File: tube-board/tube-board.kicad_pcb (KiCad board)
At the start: 2 copper layers, 25.4 x 26.4 mm, 3 parts, among them J1 Conn_01x10_Male, J2 Conn_01x01_Male

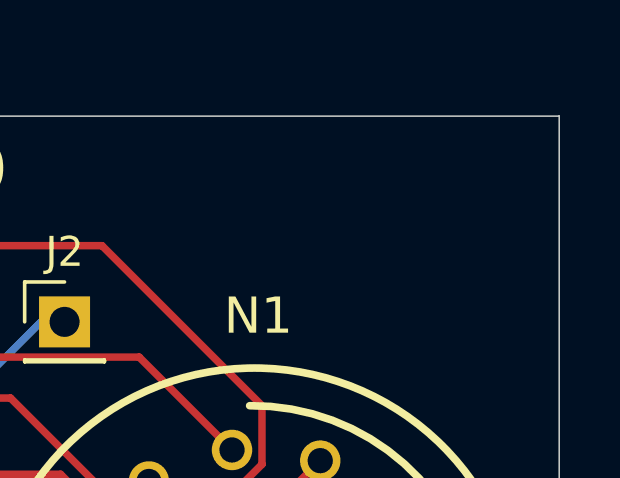
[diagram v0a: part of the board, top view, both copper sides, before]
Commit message: Add some mounting holes
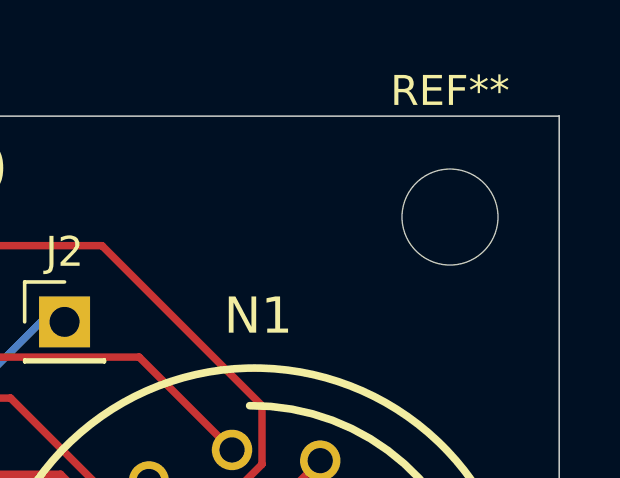
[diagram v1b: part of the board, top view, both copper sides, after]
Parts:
- added REF**: MountingHole_3.2mm_M3, MountingHole:MountingHole_3.2mm_M3, F.Cu at (100.5, 75.5)
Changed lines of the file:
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@@
-(kicad_pcb (version 20171130) (host pcbnew 5.1.12-1.fc35)
+(kicad_pcb (version 20171130) (host pcbnew 5.1.10)
   (general
     (thickness 1.6)
@@
     (tracks 42)
     (zones 0)
-    (modules 3)
+    (modules 4)
     (nets 14)
   )
@@
     (add_net "Net-(N1-PadRHDP)")
   )
+  (module MountingHole:MountingHole_3.2mm_M3 (layer F.Cu)
+    (at 100.5 75.5)
+    (descr "Mounting Hole 3.2mm, no annular, M3")
+    (tags "mounting hole 3.2mm no annular m3")
+    (attr virtual)
+    (fp_text reference REF** (at 0 -4.2) (layer F.SilkS)
+      (effects (font (size 1 1) (thickness 0.15)))
+    )
+    (fp_text value MountingHole_3.2mm_M3 (at 0 4.2) (layer F.Fab)
+      (effects (font (size 1 1) (thickness 0.15)))
+    )
+    (fp_text user %R (at 0.3 0) (layer F.Fab)
+      (effects (font (size 1 1) (thickness 0.15)))
+    )
+    (fp_circle (center 0 0) (end 3.2 0) (layer Cmts.User) (width 0.15))
+    (fp_circle (center 0 0) (end 3.45 0) (layer F.CrtYd) (width 0.05))
+    (pad 1 np_thru_hole circle (at 0 0) (size 3.2 3.2) (drill 3.2) (layers *.Cu *.Mask))
+  )
   (module nixies-us:IN-14 (layer F.Cu)
     (at 93.98 89.408 270)
@@
       (effects (font (size 1 1) (thickness 0.15)))
     )
+    (fp_line (start 1.8 -1.8) (end -1.8 -1.8) (layer F.CrtYd) (width 0.05))
+    (fp_line (start 1.8 1.8) (end 1.8 -1.8) (layer F.CrtYd) (width 0.05))
+    (fp_line (start -1.8 1.8) (end 1.8 1.8) (layer F.CrtYd) (width 0.05))
+    (fp_line (start -1.8 -1.8) (end -1.8 1.8) (layer F.CrtYd) (width 0.05))
+    (fp_line (start -1.33 -1.33) (end 0 -1.33) (layer F.SilkS) (width 0.12))
+    (fp_line (start -1.33 0) (end -1.33 -1.33) (layer F.SilkS) (width 0.12))
+    (fp_line (start -1.33 1.27) (end 1.33 1.27) (layer F.SilkS) (width 0.12))
+    (fp_line (start 1.33 1.27) (end 1.33 1.33) (layer F.SilkS) (width 0.12))
+    (fp_line (start -1.33 1.27) (end -1.33 1.33) (layer F.SilkS) (width 0.12))
+    (fp_line (start -1.33 1.33) (end 1.33 1.33) (layer F.SilkS) (width 0.12))
+    (fp_line (start -1.27 -0.635) (end -0.635 -1.27) (layer F.Fab) (width 0.1))
+    (fp_line (start -1.27 1.27) (end -1.27 -0.635) (layer F.Fab) (width 0.1))
+    (fp_line (start 1.27 1.27) (end -1.27 1.27) (layer F.Fab) (width 0.1))
+    (fp_line (start 1.27 -1.27) (end 1.27 1.27) (layer F.Fab) (width 0.1))
+    (fp_line (start -0.635 -1.27) (end 1.27 -1.27) (layer F.Fab) (width 0.1))
     (fp_text user %R (at 0 0 90) (layer F.Fab)
       (effects (font (size 1 1) (thickness 0.15)))
     )
-    (fp_line (start -0.635 -1.27) (end 1.27 -1.27) (layer F.Fab) (width 0.1))
-    (fp_line (start 1.27 -1.27) (end 1.27 1.27) (layer F.Fab) (width 0.1))
-    (fp_line (start 1.27 1.27) (end -1.27 1.27) (layer F.Fab) (width 0.1))
-    (fp_line (start -1.27 1.27) (end -1.27 -0.635) (layer F.Fab) (width 0.1))
-    (fp_line (start -1.27 -0.635) (end -0.635 -1.27) (layer F.Fab) (width 0.1))
-    (fp_line (start -1.33 1.33) (end 1.33 1.33) (layer F.SilkS) (width 0.12))
-    (fp_line (start -1.33 1.27) (end -1.33 1.33) (layer F.SilkS) (width 0.12))
-    (fp_line (start 1.33 1.27) (end 1.33 1.33) (layer F.SilkS) (width 0.12))
-    (fp_line (start -1.33 1.27) (end 1.33 1.27) (layer F.SilkS) (width 0.12))
-    (fp_line (start -1.33 0) (end -1.33 -1.33) (layer F.SilkS) (width 0.12))
-    (fp_line (start -1.33 -1.33) (end 0 -1.33) (layer F.SilkS) (width 0.12))
-    (fp_line (start -1.8 -1.8) (end -1.8 1.8) (layer F.CrtYd) (width 0.05))
-    (fp_line (start -1.8 1.8) (end 1.8 1.8) (layer F.CrtYd) (width 0.05))
-    (fp_line (start 1.8 1.8) (end 1.8 -1.8) (layer F.CrtYd) (width 0.05))
-    (fp_line (start 1.8 -1.8) (end -1.8 -1.8) (layer F.CrtYd) (width 0.05))
     (pad 1 thru_hole rect (at 0 0) (size 1.7 1.7) (drill 1) (layers *.Cu *.Mask)
       (net 11 "Net-(J2-Pad1)"))
@@
       (effects (font (size 1 1) (thickness 0.15)))
     )
+    (fp_line (start 1.8 -1.8) (end -1.8 -1.8) (layer F.CrtYd) (width 0.05))
+    (fp_line (start 1.8 24.65) (end 1.8 -1.8) (layer F.CrtYd) (width 0.05))
+    (fp_line (start -1.8 24.65) (end 1.8 24.65) (layer F.CrtYd) (width 0.05))
+    (fp_line (start -1.8 -1.8) (end -1.8 24.65) (layer F.CrtYd) (width 0.05))
+    (fp_line (start -1.33 -1.33) (end 0 -1.33) (layer F.SilkS) (width 0.12))
+    (fp_line (start -1.33 0) (end -1.33 -1.33) (layer F.SilkS) (width 0.12))
+    (fp_line (start -1.33 1.27) (end 1.33 1.27) (layer F.SilkS) (width 0.12))
+    (fp_line (start 1.33 1.27) (end 1.33 24.19) (layer F.SilkS) (width 0.12))
+    (fp_line (start -1.33 1.27) (end -1.33 24.19) (layer F.SilkS) (width 0.12))
+    (fp_line (start -1.33 24.19) (end 1.33 24.19) (layer F.SilkS) (width 0.12))
+    (fp_line (start -1.27 -0.635) (end -0.635 -1.27) (layer F.Fab) (width 0.1))
+    (fp_line (start -1.27 24.13) (end -1.27 -0.635) (layer F.Fab) (width 0.1))
+    (fp_line (start 1.27 24.13) (end -1.27 24.13) (layer F.Fab) (width 0.1))
+    (fp_line (start 1.27 -1.27) (end 1.27 24.13) (layer F.Fab) (width 0.1))
+    (fp_line (start -0.635 -1.27) (end 1.27 -1.27) (layer F.Fab) (width 0.1))
     (fp_text user %R (at 0 11.43 90) (layer F.Fab)
       (effects (font (size 1 1) (thickness 0.15)))
     )
-    (fp_line (start -0.635 -1.27) (end 1.27 -1.27) (layer F.Fab) (width 0.1))
-    (fp_line (start 1.27 -1.27) (end 1.27 24.13) (layer F.Fab) (width 0.1))
-    (fp_line (start 1.27 24.13) (end -1.27 24.13) (layer F.Fab) (width 0.1))
-    (fp_line (start -1.27 24.13) (end -1.27 -0.635) (layer F.Fab) (width 0.1))
-    (fp_line (start -1.27 -0.635) (end -0.635 -1.27) (layer F.Fab) (width 0.1))
-    (fp_line (start -1.33 24.19) (end 1.33 24.19) (layer F.SilkS) (width 0.12))
-    (fp_line (start -1.33 1.27) (end -1.33 24.19) (layer F.SilkS) (width 0.12))
-    (fp_line (start 1.33 1.27) (end 1.33 24.19) (layer F.SilkS) (width 0.12))
-    (fp_line (start -1.33 1.27) (end 1.33 1.27) (layer F.SilkS) (width 0.12))
-    (fp_line (start -1.33 0) (end -1.33 -1.33) (layer F.SilkS) (width 0.12))
-    (fp_line (start -1.33 -1.33) (end 0 -1.33) (layer F.SilkS) (width 0.12))
-    (fp_line (start -1.8 -1.8) (end -1.8 24.65) (layer F.CrtYd) (width 0.05))
-    (fp_line (start -1.8 24.65) (end 1.8 24.65) (layer F.CrtYd) (width 0.05))
-    (fp_line (start 1.8 24.65) (end 1.8 -1.8) (layer F.CrtYd) (width 0.05))
-    (fp_line (start 1.8 -1.8) (end -1.8 -1.8) (layer F.CrtYd) (width 0.05))
     (pad 10 thru_hole oval (at 0 22.86) (size 1.7 1.7) (drill 1) (layers *.Cu *.Mask)
       (net 1 "Net-(J1-Pad10)"))

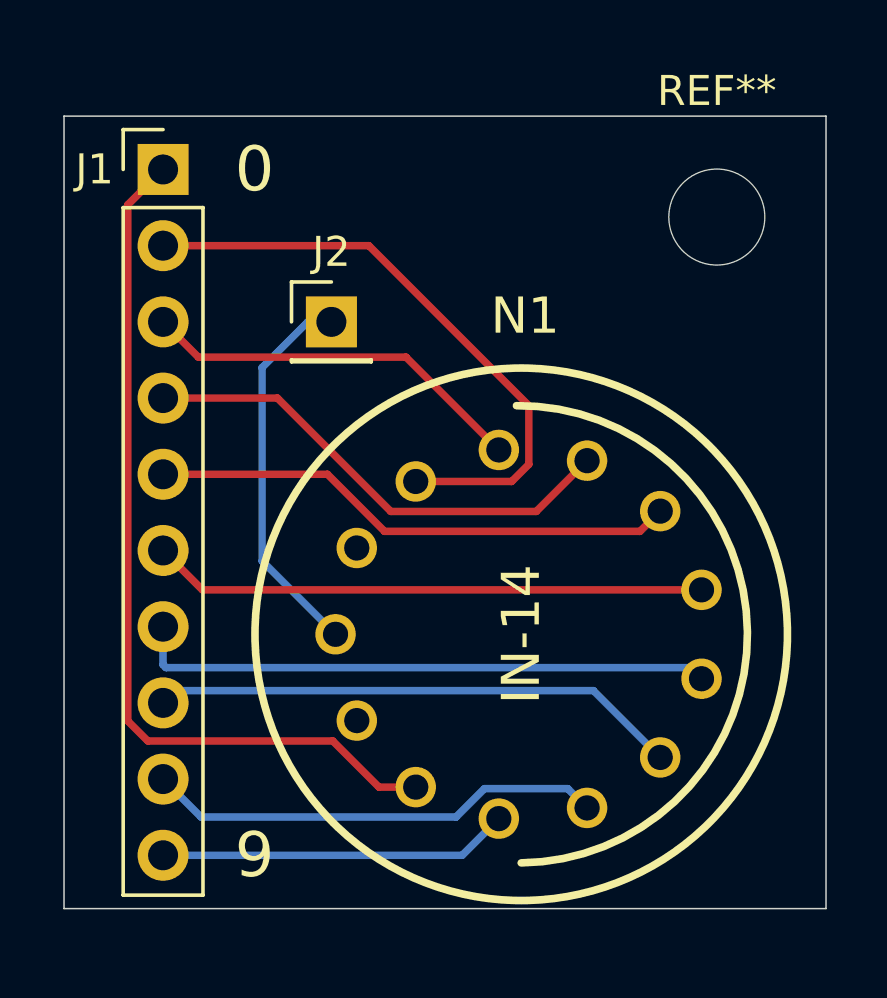
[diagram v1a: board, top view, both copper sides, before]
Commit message: tweak tube board height to not cut off silkscreen
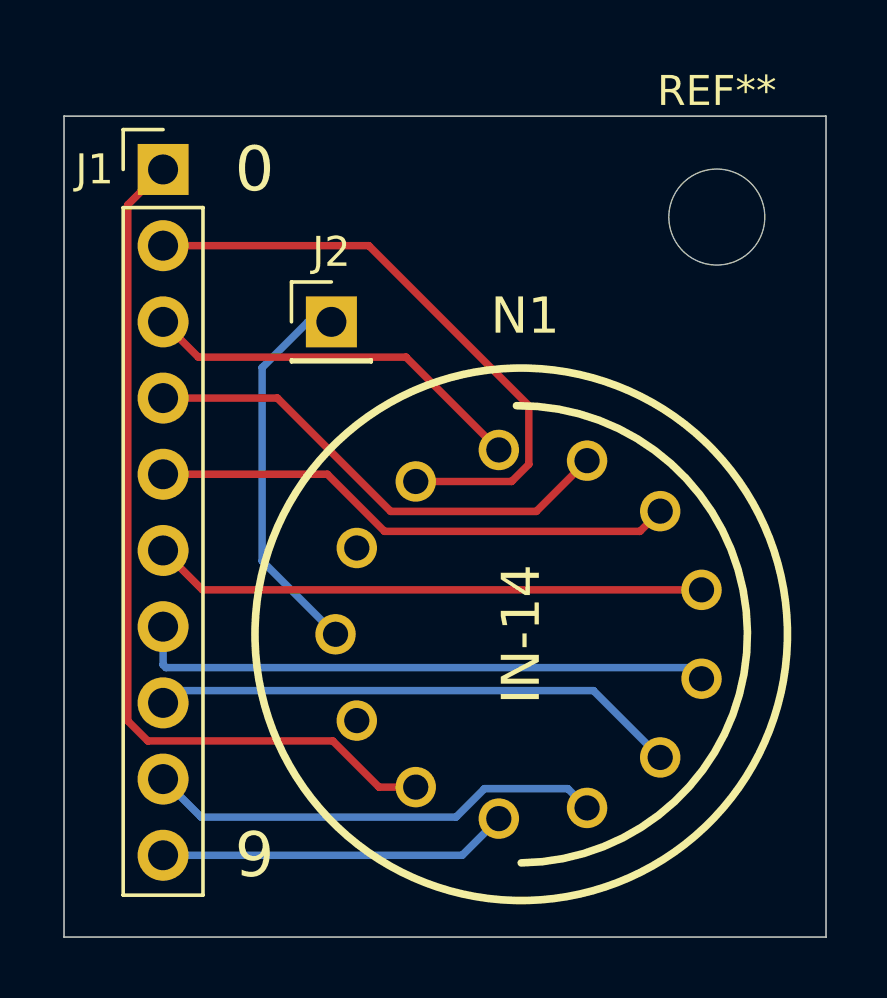
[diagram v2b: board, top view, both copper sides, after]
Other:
- board size 25.4 x 26.4 mm -> 25.4 x 27.4 mm
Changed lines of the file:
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@@
       (effects (font (size 1 1) (thickness 0.15)))
     )
+    (fp_circle (center 0 0) (end 3.45 0) (layer F.CrtYd) (width 0.05))
+    (fp_circle (center 0 0) (end 3.2 0) (layer Cmts.User) (width 0.15))
     (fp_text user %R (at 0.3 0) (layer F.Fab)
       (effects (font (size 1 1) (thickness 0.15)))
     )
-    (fp_circle (center 0 0) (end 3.2 0) (layer Cmts.User) (width 0.15))
-    (fp_circle (center 0 0) (end 3.45 0) (layer F.CrtYd) (width 0.05))
     (pad 1 np_thru_hole circle (at 0 0) (size 3.2 3.2) (drill 3.2) (layers *.Cu *.Mask))
   )
@@
       (effects (font (size 1 1) (thickness 0.15)))
     )
+    (fp_line (start -0.635 -1.27) (end 1.27 -1.27) (layer F.Fab) (width 0.1))
+    (fp_line (start 1.27 -1.27) (end 1.27 1.27) (layer F.Fab) (width 0.1))
+    (fp_line (start 1.27 1.27) (end -1.27 1.27) (layer F.Fab) (width 0.1))
+    (fp_line (start -1.27 1.27) (end -1.27 -0.635) (layer F.Fab) (width 0.1))
+    (fp_line (start -1.27 -0.635) (end -0.635 -1.27) (layer F.Fab) (width 0.1))
+    (fp_line (start -1.33 1.33) (end 1.33 1.33) (layer F.SilkS) (width 0.12))
+    (fp_line (start -1.33 1.27) (end -1.33 1.33) (layer F.SilkS) (width 0.12))
+    (fp_line (start 1.33 1.27) (end 1.33 1.33) (layer F.SilkS) (width 0.12))
+    (fp_line (start -1.33 1.27) (end 1.33 1.27) (layer F.SilkS) (width 0.12))
+    (fp_line (start -1.33 0) (end -1.33 -1.33) (layer F.SilkS) (width 0.12))
+    (fp_line (start -1.33 -1.33) (end 0 -1.33) (layer F.SilkS) (width 0.12))
+    (fp_line (start -1.8 -1.8) (end -1.8 1.8) (layer F.CrtYd) (width 0.05))
+    (fp_line (start -1.8 1.8) (end 1.8 1.8) (layer F.CrtYd) (width 0.05))
+    (fp_line (start 1.8 1.8) (end 1.8 -1.8) (layer F.CrtYd) (width 0.05))
     (fp_line (start 1.8 -1.8) (end -1.8 -1.8) (layer F.CrtYd) (width 0.05))
-    (fp_line (start 1.8 1.8) (end 1.8 -1.8) (layer F.CrtYd) (width 0.05))
-    (fp_line (start -1.8 1.8) (end 1.8 1.8) (layer F.CrtYd) (width 0.05))
-    (fp_line (start -1.8 -1.8) (end -1.8 1.8) (layer F.CrtYd) (width 0.05))
-    (fp_line (start -1.33 -1.33) (end 0 -1.33) (layer F.SilkS) (width 0.12))
-    (fp_line (start -1.33 0) (end -1.33 -1.33) (layer F.SilkS) (width 0.12))
-    (fp_line (start -1.33 1.27) (end 1.33 1.27) (layer F.SilkS) (width 0.12))
-    (fp_line (start 1.33 1.27) (end 1.33 1.33) (layer F.SilkS) (width 0.12))
-    (fp_line (start -1.33 1.27) (end -1.33 1.33) (layer F.SilkS) (width 0.12))
-    (fp_line (start -1.33 1.33) (end 1.33 1.33) (layer F.SilkS) (width 0.12))
-    (fp_line (start -1.27 -0.635) (end -0.635 -1.27) (layer F.Fab) (width 0.1))
-    (fp_line (start -1.27 1.27) (end -1.27 -0.635) (layer F.Fab) (width 0.1))
-    (fp_line (start 1.27 1.27) (end -1.27 1.27) (layer F.Fab) (width 0.1))
-    (fp_line (start 1.27 -1.27) (end 1.27 1.27) (layer F.Fab) (width 0.1))
-    (fp_line (start -0.635 -1.27) (end 1.27 -1.27) (layer F.Fab) (width 0.1))
     (fp_text user %R (at 0 0 90) (layer F.Fab)
       (effects (font (size 1 1) (thickness 0.15)))
@@
       (effects (font (size 1 1) (thickness 0.15)))
     )
+    (fp_line (start -0.635 -1.27) (end 1.27 -1.27) (layer F.Fab) (width 0.1))
+    (fp_line (start 1.27 -1.27) (end 1.27 24.13) (layer F.Fab) (width 0.1))
+    (fp_line (start 1.27 24.13) (end -1.27 24.13) (layer F.Fab) (width 0.1))
+    (fp_line (start -1.27 24.13) (end -1.27 -0.635) (layer F.Fab) (width 0.1))
+    (fp_line (start -1.27 -0.635) (end -0.635 -1.27) (layer F.Fab) (width 0.1))
+    (fp_line (start -1.33 24.19) (end 1.33 24.19) (layer F.SilkS) (width 0.12))
+    (fp_line (start -1.33 1.27) (end -1.33 24.19) (layer F.SilkS) (width 0.12))
+    (fp_line (start 1.33 1.27) (end 1.33 24.19) (layer F.SilkS) (width 0.12))
+    (fp_line (start -1.33 1.27) (end 1.33 1.27) (layer F.SilkS) (width 0.12))
+    (fp_line (start -1.33 0) (end -1.33 -1.33) (layer F.SilkS) (width 0.12))
+    (fp_line (start -1.33 -1.33) (end 0 -1.33) (layer F.SilkS) (width 0.12))
+    (fp_line (start -1.8 -1.8) (end -1.8 24.65) (layer F.CrtYd) (width 0.05))
+    (fp_line (start -1.8 24.65) (end 1.8 24.65) (layer F.CrtYd) (width 0.05))
+    (fp_line (start 1.8 24.65) (end 1.8 -1.8) (layer F.CrtYd) (width 0.05))
     (fp_line (start 1.8 -1.8) (end -1.8 -1.8) (layer F.CrtYd) (width 0.05))
-    (fp_line (start 1.8 24.65) (end 1.8 -1.8) (layer F.CrtYd) (width 0.05))
-    (fp_line (start -1.8 24.65) (end 1.8 24.65) (layer F.CrtYd) (width 0.05))
-    (fp_line (start -1.8 -1.8) (end -1.8 24.65) (layer F.CrtYd) (width 0.05))
-    (fp_line (start -1.33 -1.33) (end 0 -1.33) (layer F.SilkS) (width 0.12))
-    (fp_line (start -1.33 0) (end -1.33 -1.33) (layer F.SilkS) (width 0.12))
-    (fp_line (start -1.33 1.27) (end 1.33 1.27) (layer F.SilkS) (width 0.12))
-    (fp_line (start 1.33 1.27) (end 1.33 24.19) (layer F.SilkS) (width 0.12))
-    (fp_line (start -1.33 1.27) (end -1.33 24.19) (layer F.SilkS) (width 0.12))
-    (fp_line (start -1.33 24.19) (end 1.33 24.19) (layer F.SilkS) (width 0.12))
-    (fp_line (start -1.27 -0.635) (end -0.635 -1.27) (layer F.Fab) (width 0.1))
-    (fp_line (start -1.27 24.13) (end -1.27 -0.635) (layer F.Fab) (width 0.1))
-    (fp_line (start 1.27 24.13) (end -1.27 24.13) (layer F.Fab) (width 0.1))
-    (fp_line (start 1.27 -1.27) (end 1.27 24.13) (layer F.Fab) (width 0.1))
-    (fp_line (start -0.635 -1.27) (end 1.27 -1.27) (layer F.Fab) (width 0.1))
     (fp_text user %R (at 0 11.43 90) (layer F.Fab)
       (effects (font (size 1 1) (thickness 0.15)))
@@
     )
   )
-  (dimension 26.416 (width 0.15) (layer Dwgs.User)
-    (gr_text "26.416 mm" (at 75.916001 85.344 270) (layer Dwgs.User)
+  (dimension 27.364 (width 0.15) (layer Dwgs.User)
+    (gr_text "27.364 mm" (at 75.916001 85.818 270) (layer Dwgs.User)
       (effects (font (size 1 1) (thickness 0.15)))
     )
-    (feature1 (pts (xy 77.724 98.552) (xy 76.62958 98.552)))
+    (feature1 (pts (xy 77.724 99.5) (xy 76.62958 99.5)))
     (feature2 (pts (xy 77.724 72.136) (xy 76.62958 72.136)))
-    (crossbar (pts (xy 77.216001 72.136) (xy 77.216001 98.552)))
-    (arrow1a (pts (xy 77.216001 98.552) (xy 76.62958 97.425496)))
-    (arrow1b (pts (xy 77.216001 98.552) (xy 77.802422 97.425496)))
+    (crossbar (pts (xy 77.216001 72.136) (xy 77.216001 99.5)))
+    (arrow1a (pts (xy 77.216001 99.5) (xy 76.62958 98.373496)))
+    (arrow1b (pts (xy 77.216001 99.5) (xy 77.802422 98.373496)))
     (arrow2a (pts (xy 77.216001 72.136) (xy 76.62958 73.262504)))
     (arrow2b (pts (xy 77.216001 72.136) (xy 77.802422 73.262504)))
@@
   )
   (gr_line (start 78.74 72.136) (end 104.14 72.136) (layer Edge.Cuts) (width 0.05))
-  (gr_line (start 104.14 98.552) (end 104.14 72.136) (layer Edge.Cuts) (width 0.05))
-  (gr_line (start 78.74 98.552) (end 104.14 98.552) (layer Edge.Cuts) (width 0.05))
-  (gr_line (start 78.74 72.136) (end 78.74 98.552) (layer Edge.Cuts) (width 0.05))
+  (gr_line (start 104.14 99.5) (end 104.14 72.136) (layer Edge.Cuts) (width 0.05))
+  (gr_line (start 78.74 99.5) (end 104.14 99.5) (layer Edge.Cuts) (width 0.05))
+  (gr_line (start 78.74 72.136) (end 78.74 99.5) (layer Edge.Cuts) (width 0.05))
   (gr_text 9 (at 85.09 96.774) (layer F.SilkS)
     (effects (font (size 1.5 1.5) (thickness 0.3)))
